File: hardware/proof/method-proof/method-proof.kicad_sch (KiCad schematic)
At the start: 19 parts, among them J1 5V_IN, J2 OUT, J3 PA1, U1 MCP1700T-3302E/TT, U2 MSPS003F4SPW20R

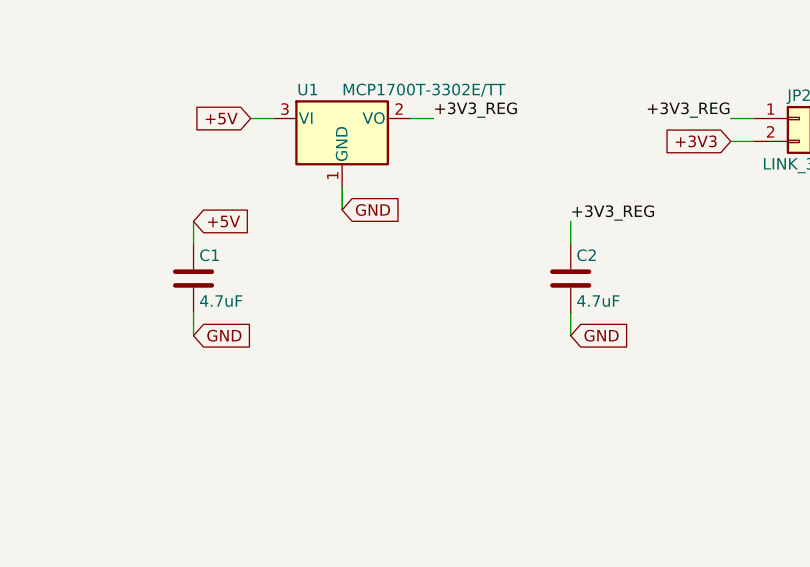
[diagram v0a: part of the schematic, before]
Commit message: hardware(method-proof): prove the value-critical circuits before layout: circuit-proof.md, the netlist export and the calculation script
Not for manufacture. Five rows: the status LED drive stage, the regulator's
capacitors, the controller's supply capacitor, the 3.3 V rail against the
regulator's and the controller's ranges, and the LED node against PA0's limit.
The regulator's and the supply's capacitors move to KEMET polymer tantalum and
ceramic parts whose datasheets bound what the regulator and the controller ask
of them. Its Not bounded by a source section lists the conditions no datasheet
read states as a limit.

Co-Authored-By: Claude Sonnet 5.5 <noreply@anthropic.com>
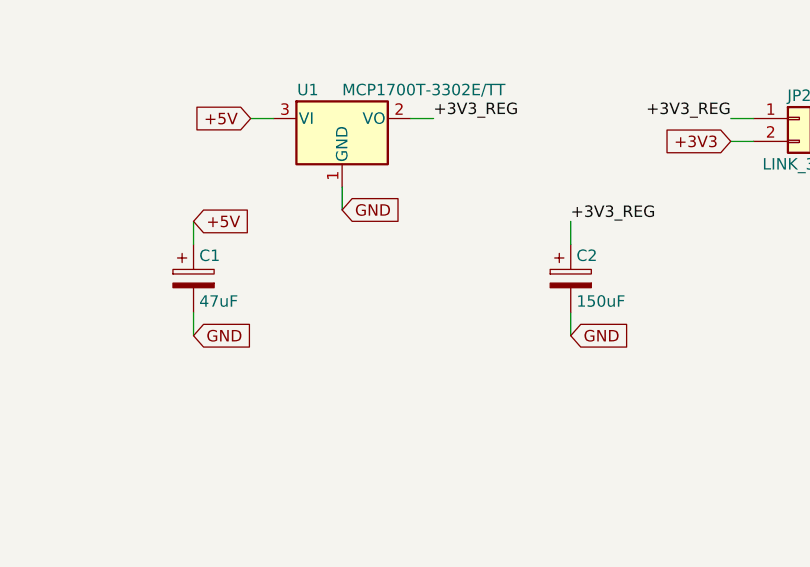
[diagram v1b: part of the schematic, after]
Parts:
- C1: value 4.7uF -> 47uF; footprint Capacitor_SMD:C_0805_2012Metric -> Capacitor_Tantalum_SMD:CP_EIA-3528-21_Kemet-B; symbol Device:C -> Device:C_Polarized; MPN C0805C475K4RACTU -> T520B476M010ATE035; Rating 16V -> 10V
- C2: value 4.7uF -> 150uF; footprint Capacitor_SMD:C_0805_2012Metric -> Capacitor_Tantalum_SMD:CP_EIA-3528-21_Kemet-B; symbol Device:C -> Device:C_Polarized; LCSC C9100008 -> C9100014; MPN C0805C475K4RACTU -> T520B157M006ATE025; Rating 16V -> 6.3V
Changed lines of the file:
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@@
 		))
 	(symbol
-		(lib_id "Device:C")
+		(lib_id "Device:C_Polarized")
 		(at 97.79 68.58 0)
 		(unit 1)
@@
 			)
 		)
-		(property "Value" "4.7uF"
+		(property "Value" "47uF"
 			(at 98.425 71.12 0)
 			(effects
@@
 			)
 		)
-		(property "Footprint" "Capacitor_SMD:C_0805_2012Metric"
+		(property "Footprint" "Capacitor_Tantalum_SMD:CP_EIA-3528-21_Kemet-B"
 			(at 97.79 68.58 0)
 			(hide yes)
@@
 			)
 		)
-		(property "Datasheet" "https://content.kemet.com/datasheets/KEM_C1002_X7R_SMD.pdf"
+		(property "Datasheet" "https://search.kemet.com/download/specsheet/T520B476M010ATE035"
 			(at 97.79 68.58 0)
 			(hide yes)
@@
 			)
 		)
-		(property "MPN" "C0805C475K4RACTU"
+		(property "MPN" "T520B476M010ATE035"
 			(at 97.79 68.58 0)
 			(hide yes)
@@
 			)
 		)
-		(property "Rating" "16V"
+		(property "Rating" "10V"
 			(at 97.79 68.58 0)
 			(hide yes)
@@
 		))
 	(symbol
-		(lib_id "Device:C")
+		(lib_id "Device:C_Polarized")
 		(at 139.7 68.58 0)
 		(unit 1)
@@
 			)
 		)
-		(property "Value" "4.7uF"
+		(property "Value" "150uF"
 			(at 140.335 71.12 0)
 			(effects
@@
 			)
 		)
-		(property "Footprint" "Capacitor_SMD:C_0805_2012Metric"
+		(property "Footprint" "Capacitor_Tantalum_SMD:CP_EIA-3528-21_Kemet-B"
 			(at 139.7 68.58 0)
 			(hide yes)
@@
 			)
 		)
-		(property "Datasheet" "https://content.kemet.com/datasheets/KEM_C1002_X7R_SMD.pdf"
+		(property "Datasheet" "https://search.kemet.com/download/specsheet/T520B157M006ATE025"
 			(at 139.7 68.58 0)
 			(hide yes)
@@
 			)
 		)
-		(property "LCSC" "C9100008"
+		(property "LCSC" "C9100014"
 			(at 139.7 68.58 0)
 			(hide yes)
@@
 			)
 		)
-		(property "MPN" "C0805C475K4RACTU"
+		(property "MPN" "T520B157M006ATE025"
 			(at 139.7 68.58 0)
 			(hide yes)
@@
 			)
 		)
-		(property "Rating" "16V"
+		(property "Rating" "6.3V"
 			(at 139.7 68.58 0)
 			(hide yes)

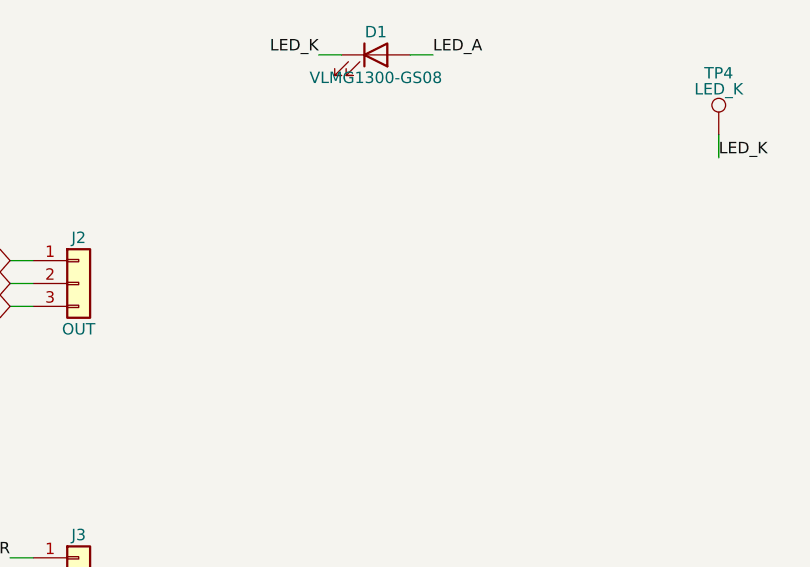
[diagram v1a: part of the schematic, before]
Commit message: hardware(method-proof): add the filter capacitors C4 and C5 at the output header and refresh the netlist export, the records and the calculation log
Not for manufacture. No requirement of either capacitor's value comes from a
datasheet, so circuit-proof.md lists them as not value-critical; the exported
netlist and the proof's log are regenerated and the proof still ends ALL MET.

Co-Authored-By: Claude Sonnet 5.5 <noreply@anthropic.com>
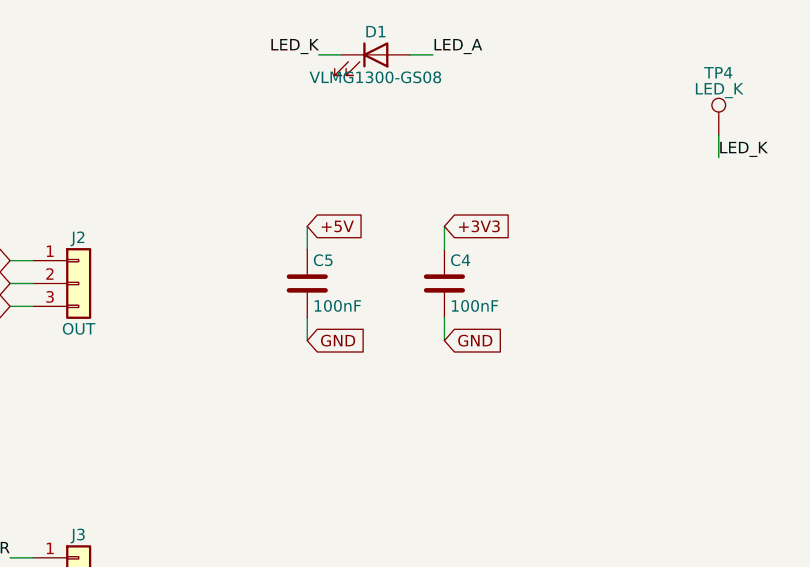
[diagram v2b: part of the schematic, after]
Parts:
- added C4, C5: 100nF, Capacitor_SMD:C_0603_1608Metric, symbol Device:C
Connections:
- net +3V3: now also C4.1
- net +5V: now also C5.1
- net GND: now also C4.2, C5.2

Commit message: hardware(method-proof): bring the footprints into step with their symbols and libraries: the symbols' fields, references on the fabrication layer, test points from the design's own library
Not for manufacture. Done with KiCad's scripting on the closed board, as the method
describes for what Konnect cannot do: each footprint carries its symbol's
description, datasheet and part fields, the mounting holes' BOM attribute follows
their symbols', the references move to the fabrication layers so no silkscreen
rule reaches them, and the four test points take the design's own footprint
library, whose copy Konnect can refresh from. The layout check reports no
violation but the unrouted connections.

Co-Authored-By: Claude Sonnet 5.5 <noreply@anthropic.com>
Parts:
- TP1, TP2, TP3, TP4: footprint TestPoint:TestPoint_Pad_D1.0mm -> method-proof:TestPoint_Pad_D1.0mm
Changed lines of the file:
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@@
 			)
 		)
-		(property "Footprint" "TestPoint:TestPoint_Pad_D1.0mm"
+		(property "Footprint" "method-proof:TestPoint_Pad_D1.0mm"
 			(at 50.8 31.75 0)
 			(hide yes)
@@
 			)
 		)
-		(property "Footprint" "TestPoint:TestPoint_Pad_D1.0mm"
+		(property "Footprint" "method-proof:TestPoint_Pad_D1.0mm"
 			(at 139.7 31.75 0)
 			(hide yes)
@@
 			)
 		)
-		(property "Footprint" "TestPoint:TestPoint_Pad_D1.0mm"
+		(property "Footprint" "method-proof:TestPoint_Pad_D1.0mm"
 			(at 200.66 31.75 0)
 			(hide yes)
@@
 			)
 		)
-		(property "Footprint" "TestPoint:TestPoint_Pad_D1.0mm"
+		(property "Footprint" "method-proof:TestPoint_Pad_D1.0mm"
 			(at 96.52 135.89 0)
 			(hide yes)

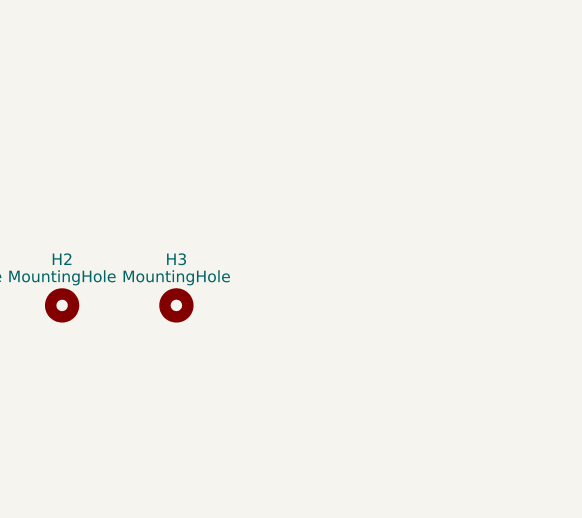
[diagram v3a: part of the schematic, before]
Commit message: fix(hardware): give the tracked proof designs the three fiducials a side with surface-mount parts needs [SOL-PRE-ORDER-CHECK-FIDUCIALS-AND-POLARITY-MARKS.C5]
Co-Authored-By: Claude Sonnet 5.5 <noreply@anthropic.com>
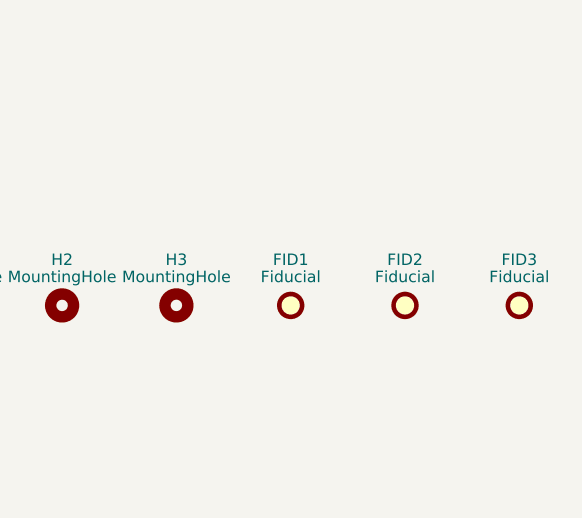
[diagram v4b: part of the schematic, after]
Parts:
- added FID1, FID2, FID3: Fiducial, Fiducial:Fiducial_1mm_Mask2mm, symbol Mechanical:Fiducial
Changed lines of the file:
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@@
+	)
+	(symbol
+		(lib_id "Mechanical:Fiducial")
+		(at 266.7 165.1 0)
+		(unit 1)
+		(in_bom no)
+		(on_board yes)
+		(dnp no)
+		(property "Reference" "FID1"
+			(at 266.7 160.02 0)
+			(effects
+				(font
+					(size 1.27 1.27)
+				)
+			)
+		)
+		(property "Value" "Fiducial"
+			(at 266.7 161.925 0)
+			(effects
+				(font
+					(size 1.27 1.27)
+				)
+			)
+		)
+		(property "Footprint" "Fiducial:Fiducial_1mm_Mask2mm"
+			(at 266.7 165.1 0)
+			(hide yes)
+			(effects
+				(font
+					(size 1.27 1.27)
+				)
+			)
+		)
+		(property "Datasheet" ""
+			(at 266.7 165.1 0)
+			(hide yes)
+			(effects
+				(font
+					(size 1.27 1.27)
+				)
+			)
+		)
+		(property "Description" "Fiducial Marker"
+			(at 266.7 165.1 0)
+			(hide yes)
+			(effects
+				(font
+					(size 1.27 1.27)
+				)
+			)
+		)
+		(property "LCSC" "C9100016"
+			(at 266.7 165.1 0)
+			(hide yes)
+			(effects
+				(font
+					(size 1.27 1.27)
+				)
+			)
+		)
+		(instances
+			(project "method-proof"
+				(path "/53bfab0d-8ce9-43a6-8b41-74dc1b65bed5"
+					(reference "FID1")
+					(unit 1)
+				)
+			)
+		)
+	)
+	(symbol
+		(lib_id "Mechanical:Fiducial")
+		(at 279.4 165.1 0)
+		(unit 1)
+		(in_bom no)
+		(on_board yes)
+		(dnp no)
+		(property "Reference" "FID2"
+			(at 279.4 160.02 0)
+			(effects
+				(font
+					(size 1.27 1.27)
+				)
+			)
+		)
+		(property "Value" "Fiducial"
+			(at 279.4 161.925 0)
+			(effects
+				(font
+					(size 1.27 1.27)
+				)
+			)
+		)
+		(property "Footprint" "Fiducial:Fiducial_1mm_Mask2mm"
+			(at 279.4 165.1 0)
+			(hide yes)
+			(effects
+				(font
+					(size 1.27 1.27)
+				)
+			)
+		)
+		(property "Datasheet" ""
+			(at 279.4 165.1 0)
+			(hide yes)
+			(effects
+				(font
+					(size 1.27 1.27)
+				)
+			)
+		)
+		(property "Description" "Fiducial Marker"
+			(at 279.4 165.1 0)
+			(hide yes)
+			(effects
+				(font
+					(size 1.27 1.27)
+				)
+			)
+		)
+		(property "LCSC" "C9100016"
+			(at 279.4 165.1 0)
+			(hide yes)
+			(effects
+				(font
+					(size 1.27 1.27)
+				)
+			)
+		)
+		(instances
+			(project "method-proof"
+				(path "/53bfab0d-8ce9-43a6-8b41-74dc1b65bed5"
+					(reference "FID2")
+					(unit 1)
+				)
+			)
+		)
+	)
+	(symbol
+		(lib_id "Mechanical:Fiducial")
+		(at 292.1 165.1 0)
+		(unit 1)
+		(in_bom no)
+		(on_board yes)
+		(dnp no)
+		(property "Reference" "FID3"
+			(at 292.1 160.02 0)
+			(effects
+				(font
+					(size 1.27 1.27)
+				)
+			)
+		)
+		(property "Value" "Fiducial"
+			(at 292.1 161.925 0)
+			(effects
+				(font
+					(size 1.27 1.27)
+				)
+			)
+		)
+		(property "Footprint" "Fiducial:Fiducial_1mm_Mask2mm"
+			(at 292.1 165.1 0)
+			(hide yes)
+			(effects
+				(font
+					(size 1.27 1.27)
+				)
+			)
+		)
+		(property "Datasheet" ""
+			(at 292.1 165.1 0)
+			(hide yes)
+			(effects
+				(font
+					(size 1.27 1.27)
+				)
+			)
+		)
+		(property "Description" "Fiducial Marker"
+			(at 292.1 165.1 0)
+			(hide yes)
+			(effects
+				(font
+					(size 1.27 1.27)
+				)
+			)
+		)
+		(property "LCSC" "C9100016"
+			(at 292.1 165.1 0)
+			(hide yes)
+			(effects
+				(font
+					(size 1.27 1.27)
+				)
+			)
+		)
+		(instances
+			(project "method-proof"
+				(path "/53bfab0d-8ce9-43a6-8b41-74dc1b65bed5"
+					(reference "FID3")
+					(unit 1)
+				)
+			)
+		)
 	)
 	(symbol
